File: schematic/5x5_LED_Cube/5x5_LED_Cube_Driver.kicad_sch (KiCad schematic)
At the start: 23 parts, among them J1 Power, J2 Adafruit_Micro_SD_Card_SPI_SD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, J3 Layers, Q1 DMG2305UX, Q2 DMG2305UX, Q3 DMG2305UX, Q4 DMG2305UX, Q5 DMG2305UX, U1 TLC5940NT, U2 TLC5940NT, U3 Pico

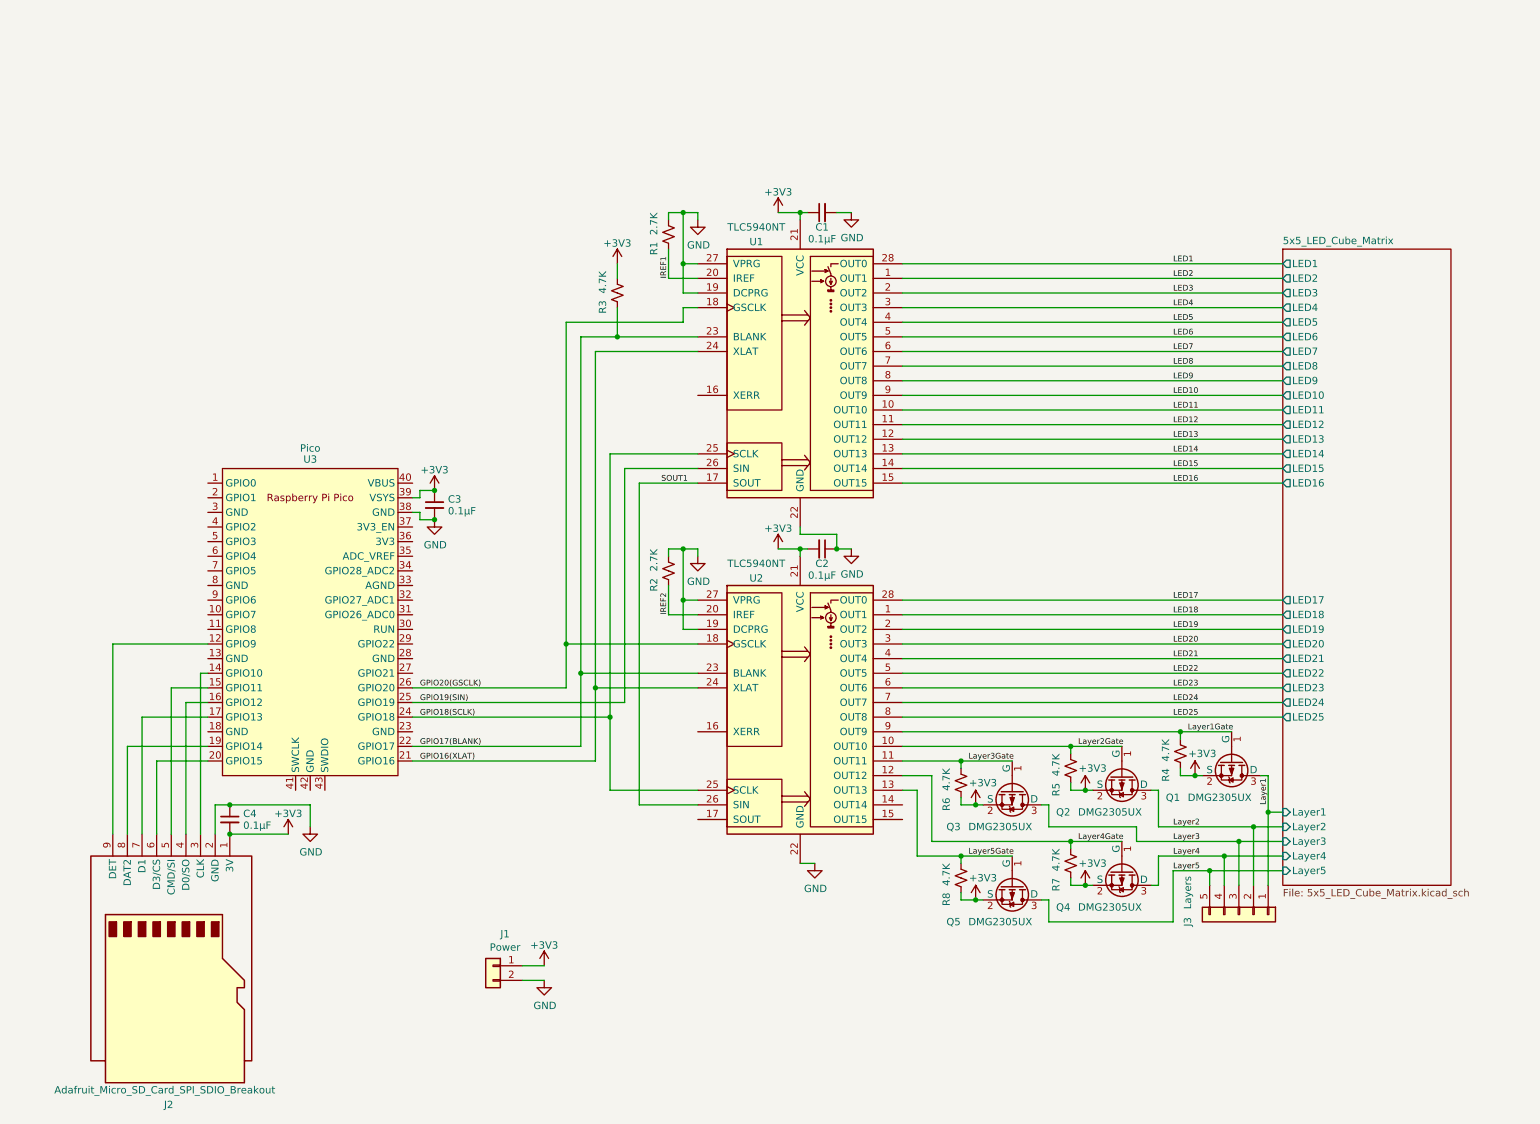
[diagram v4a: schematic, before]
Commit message: Updated schematic to use the Pico for power
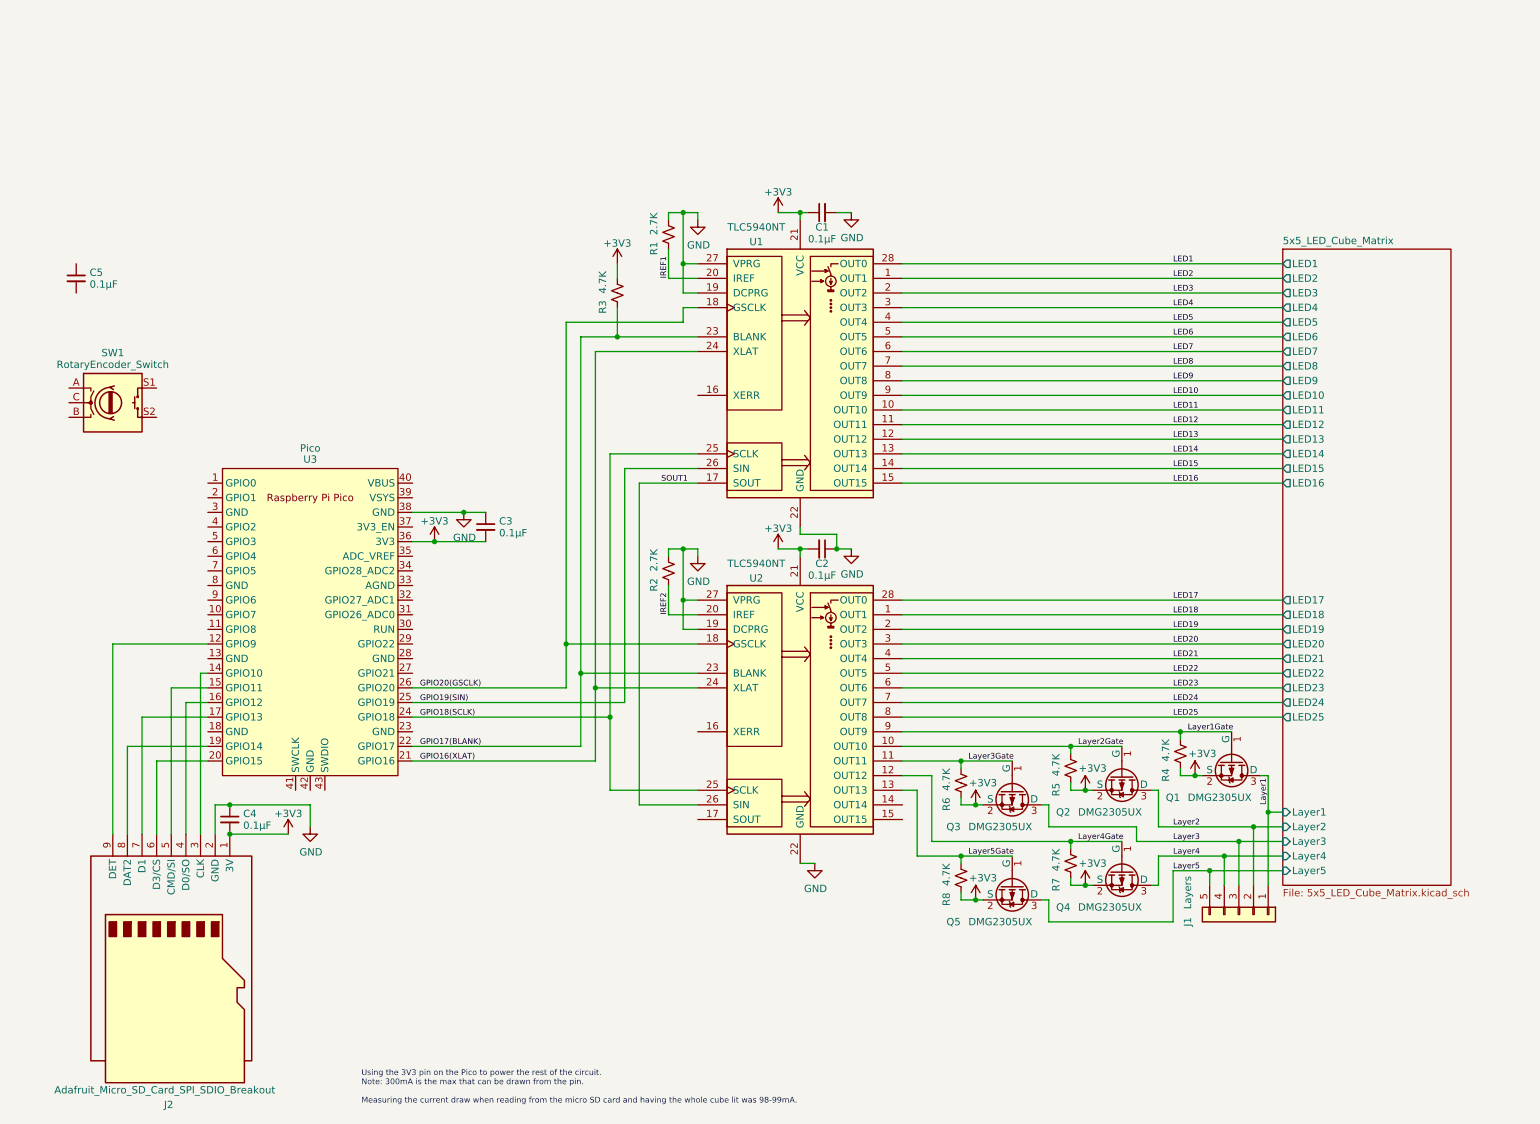
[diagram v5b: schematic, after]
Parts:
- removed J1: Power, Connector_PinSocket_2.54mm:PinSocket_1x02_P2.54mm_Vertical, symbol Connector_Generic:Conn_01x02
- added C5: 0.1µF, Capacitor_SMD:C_0402_1005Metric_Pad0.74x0.62mm_HandSolder, symbol Device:C_Small
- added SW1: RotaryEncoder_Switch, symbol Device:RotaryEncoder_Switch
- renumbered J3 to J1
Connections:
- net +3V3: now also C3.2, U3.36 (3V3); no longer C3.1, U3.39 (VSYS)
- net GND: now also C3.1; no longer C3.2
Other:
- note added: "Using the 3V3 pin on the Pico to power the rest of the circuit. Note: 300mA is the max that can be drawn from the pin. Measuring the current draw when reading from the micro SD card and having the whole cube lit was 98-99mA."
- moved on the sheet: C3

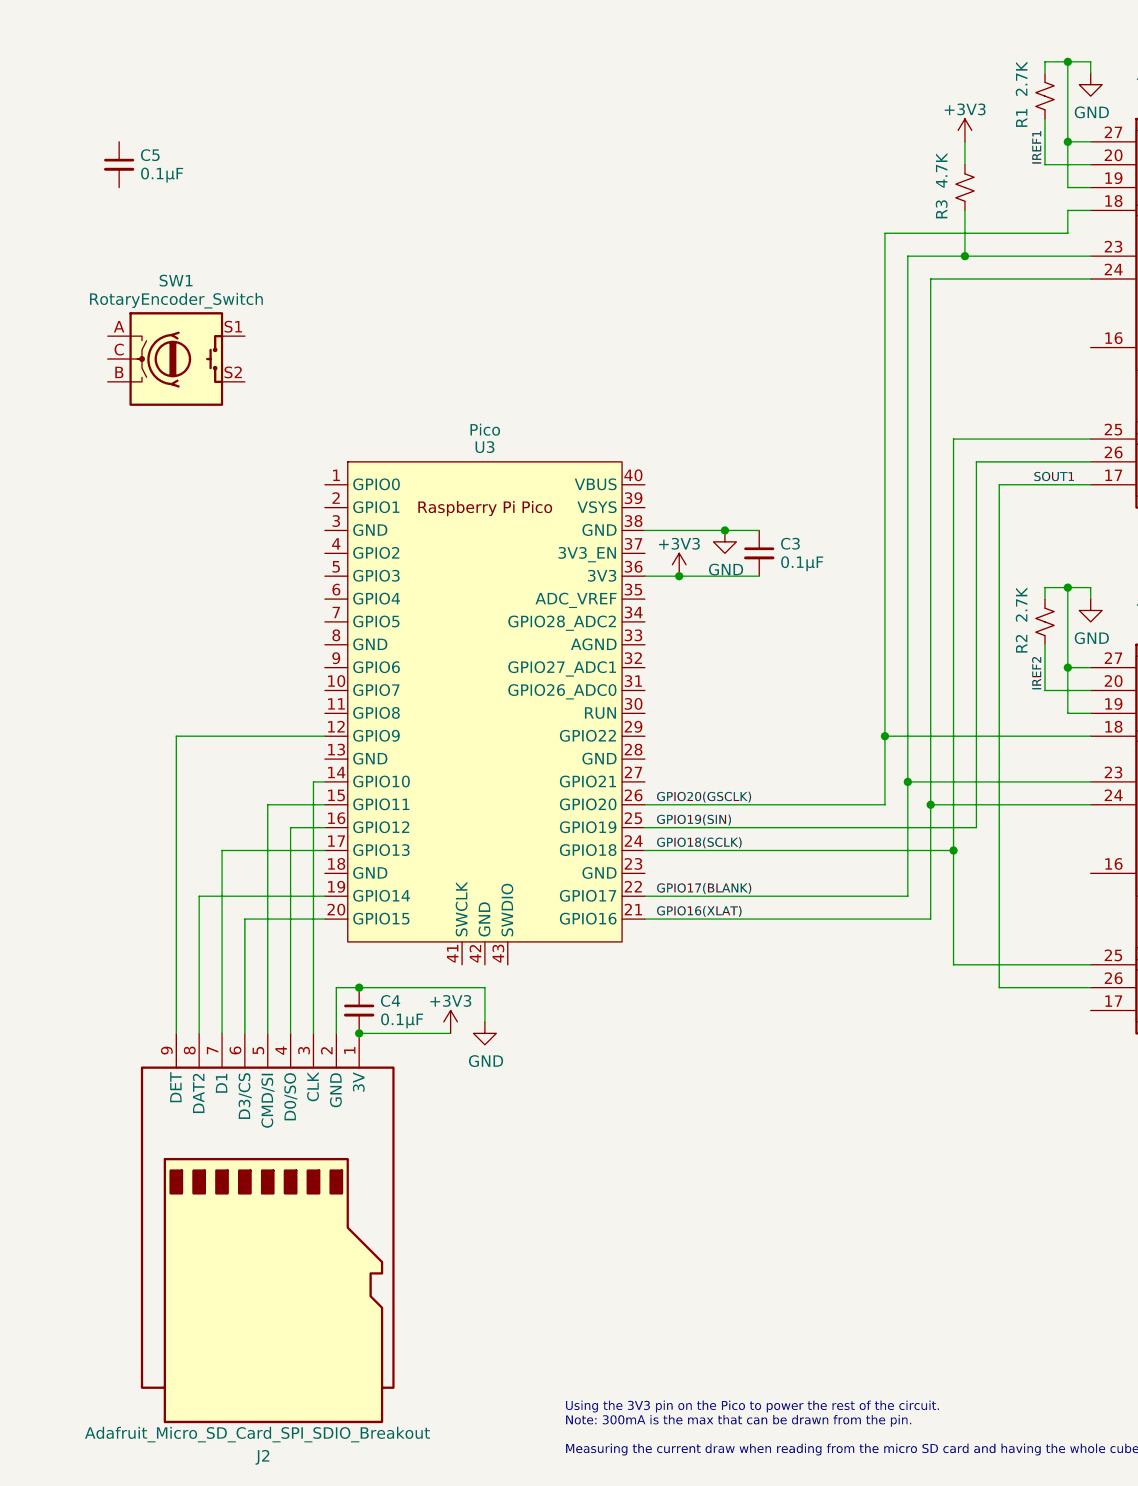
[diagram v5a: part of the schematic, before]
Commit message: Added connections for the rotary encoder and pin socker for the oled display
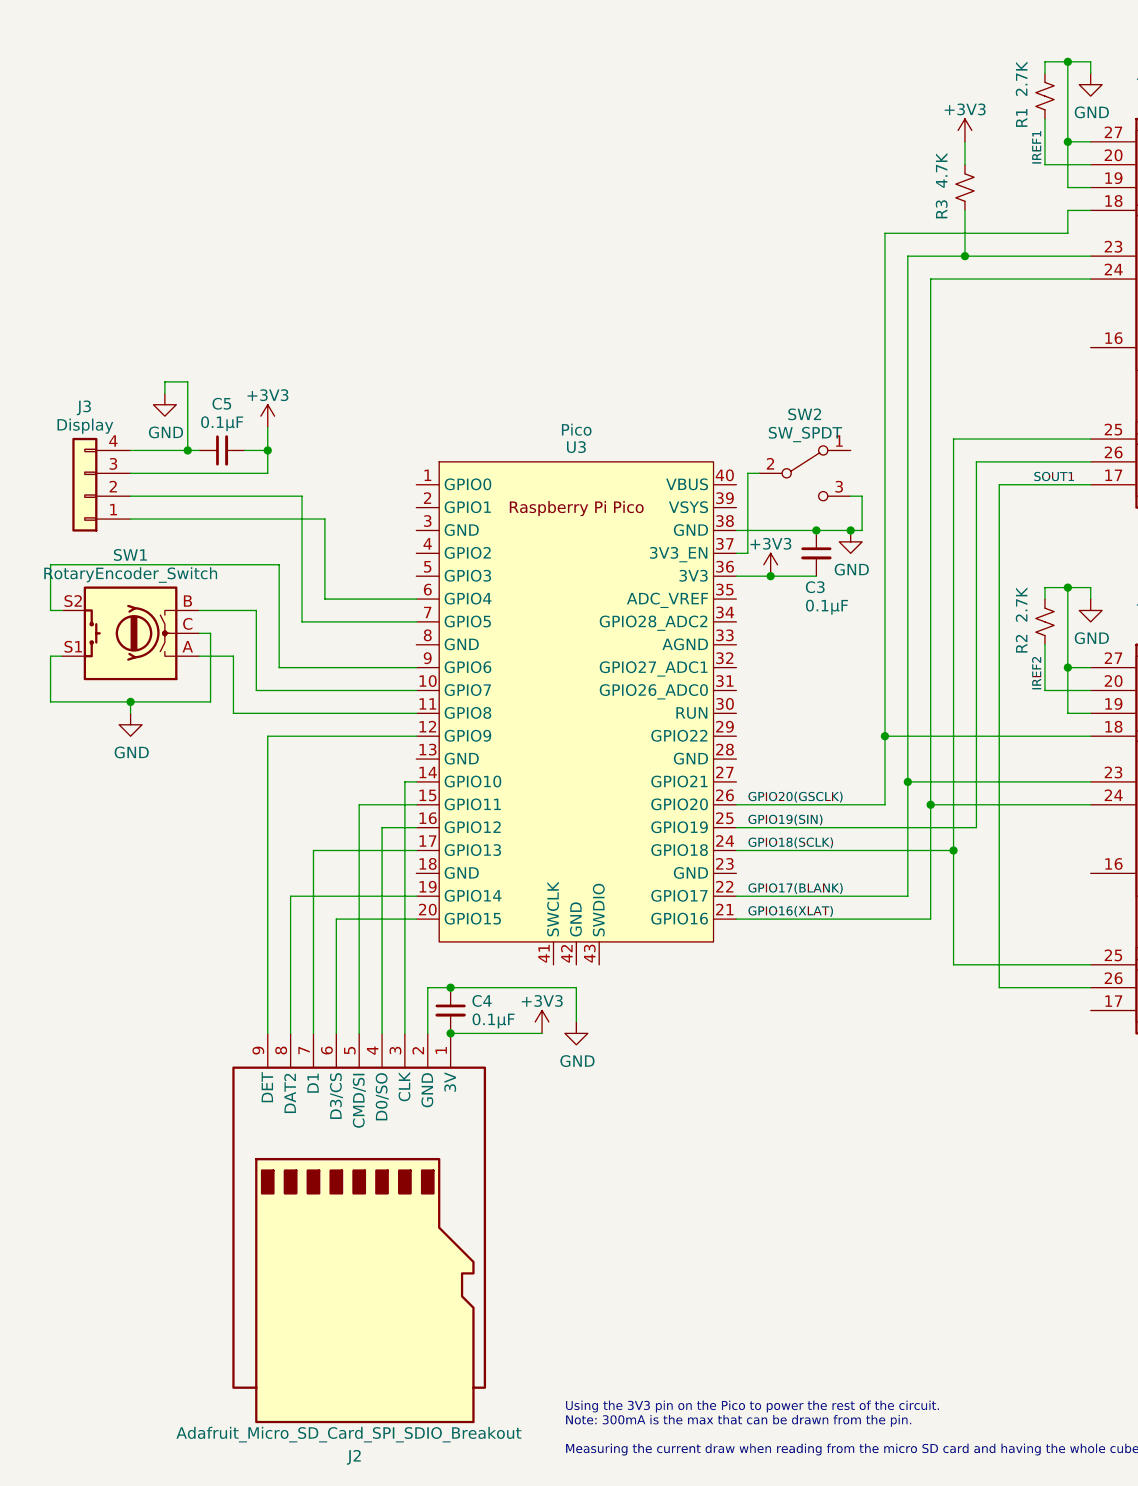
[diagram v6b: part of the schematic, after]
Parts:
- added J3: Display, symbol Connector_Generic:Conn_01x04
- added SW2: SW_SPDT, Connector_PinSocket_2.54mm:PinSocket_1x03_P2.54mm_Vertical, symbol Switch:SW_SPDT
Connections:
- net +3V3: now also C5.2, J3.3 (Pin_3)
- net GND: now also C5.1, SW1.C, SW1.S1, J3.4 (Pin_4), SW2.3 (C)
- net at SW1.A: now also U3.11 (GPIO8)
- net at SW1.B: now also U3.10 (GPIO7)
- net at SW1.S2: now also U3.9 (GPIO6)
- net at U3.37 (3V3_EN): now also SW2.2 (B)
- net at U3.6 (GPIO4): now also J3.1 (Pin_1)
- net at U3.7 (GPIO5): now also J3.2 (Pin_2)
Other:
- moved on the sheet: C3, C4, C5, J2, SW1, U3
